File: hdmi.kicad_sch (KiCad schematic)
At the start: 24 parts, among them U14 NTS0102_XSON, U17 PI3HDX511DZLE, U18 74LVC1T45GM

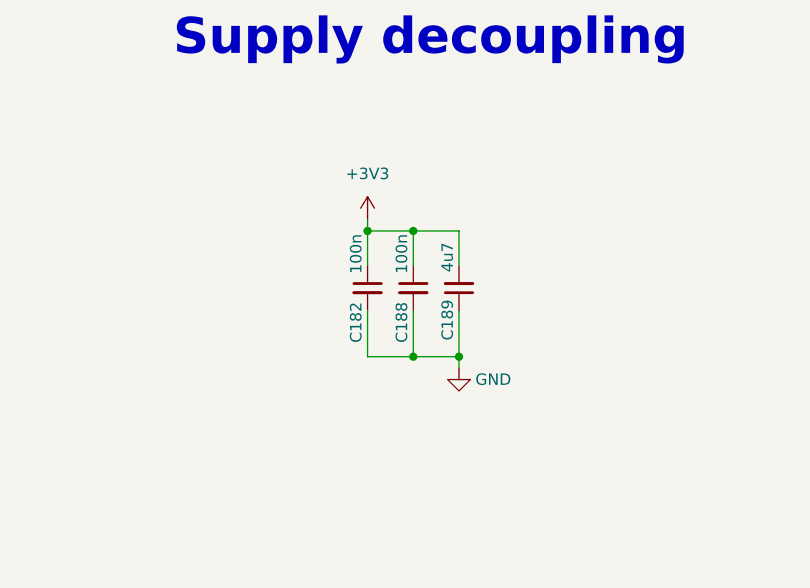
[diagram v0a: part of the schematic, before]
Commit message: [#55860] Add HDMI ferrite bead
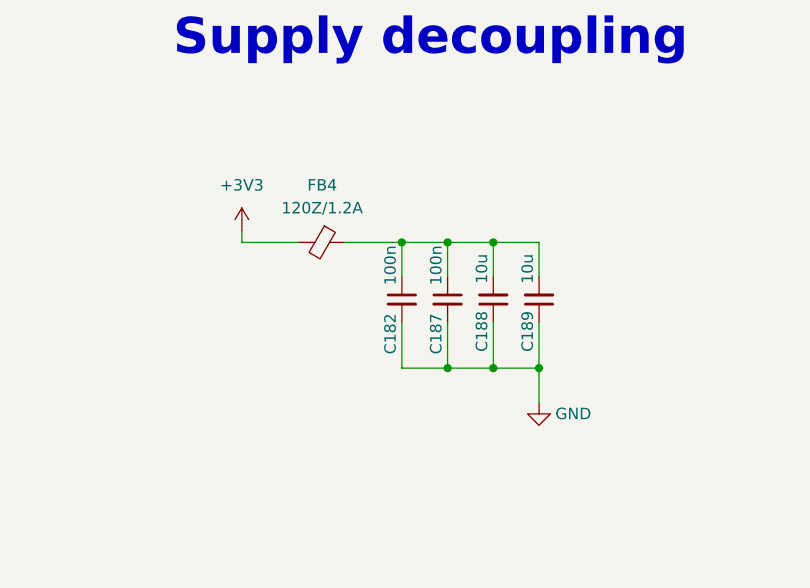
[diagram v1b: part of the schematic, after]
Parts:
- removed C188: C_100n_0201, antmicro-footprints:C_0201, symbol antmicroCapacitorsmisc:C_100n_0201
- removed C189: C_4u7_0402, antmicro-footprints:C_0402_1005Metric, symbol antmicroCapacitors0402:C_4u7_0402
- added C187: C_100n_0201, antmicro-footprints:C_0201, symbol antmicroCapacitorsmisc:C_100n_0201
- added C188, C189: C_10u_10V_0402, antmicro-footprints:C_0402_1005Metric, symbol antmicroCapacitors0402:C_10u_10V_0402
- added FB4: FB_120Z_1.2A_TDK-MPZ_0402, antmicro-footprints:FB_0402_1005Metric, symbol antmicroFerriteBeadsandChips:FB_120Z_1.2A_TDK-MPZ_0402
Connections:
- net +3V3: now also FB4.2; no longer C182.1
- net GND: now also C187.2, C188.1, C189.1
- new net: C182.1, C187.1, C188.2, C189.2, FB4.1

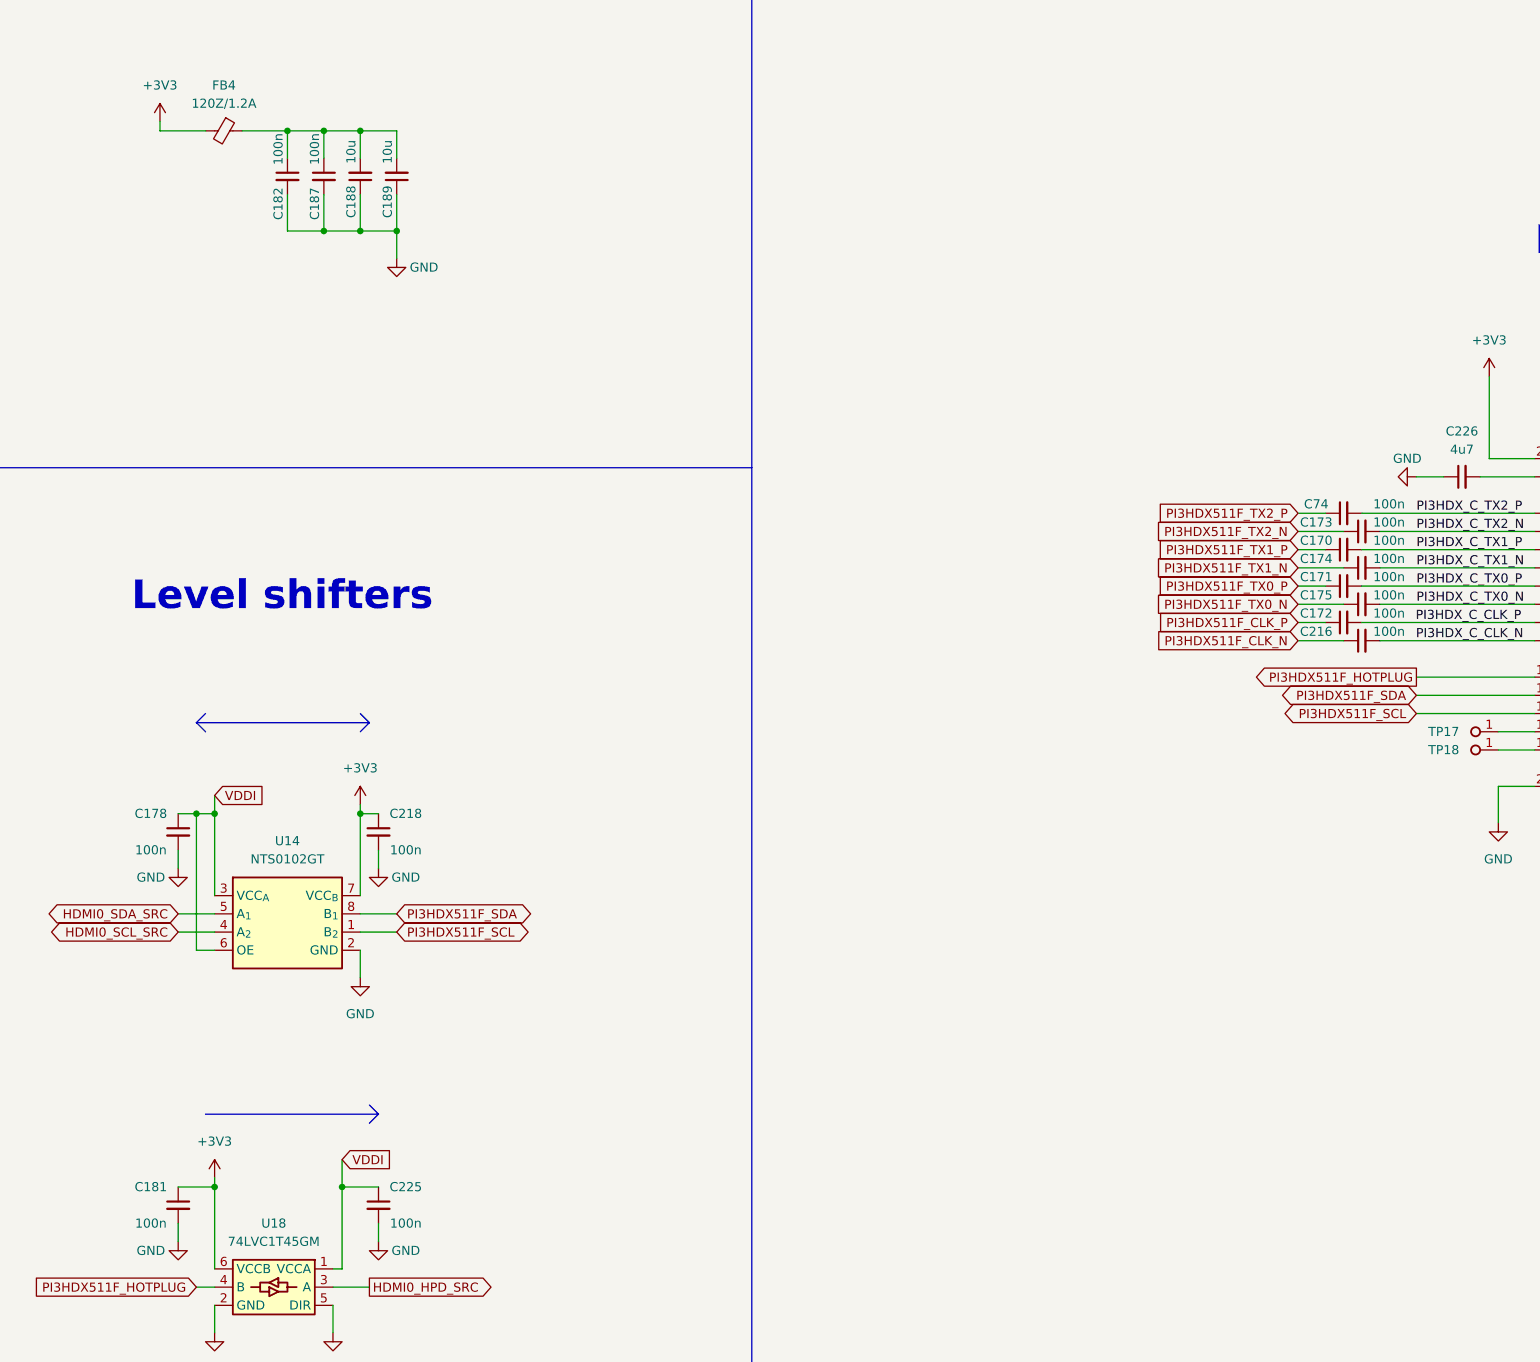
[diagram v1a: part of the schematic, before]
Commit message: [#55992] Replace 100n capacitors
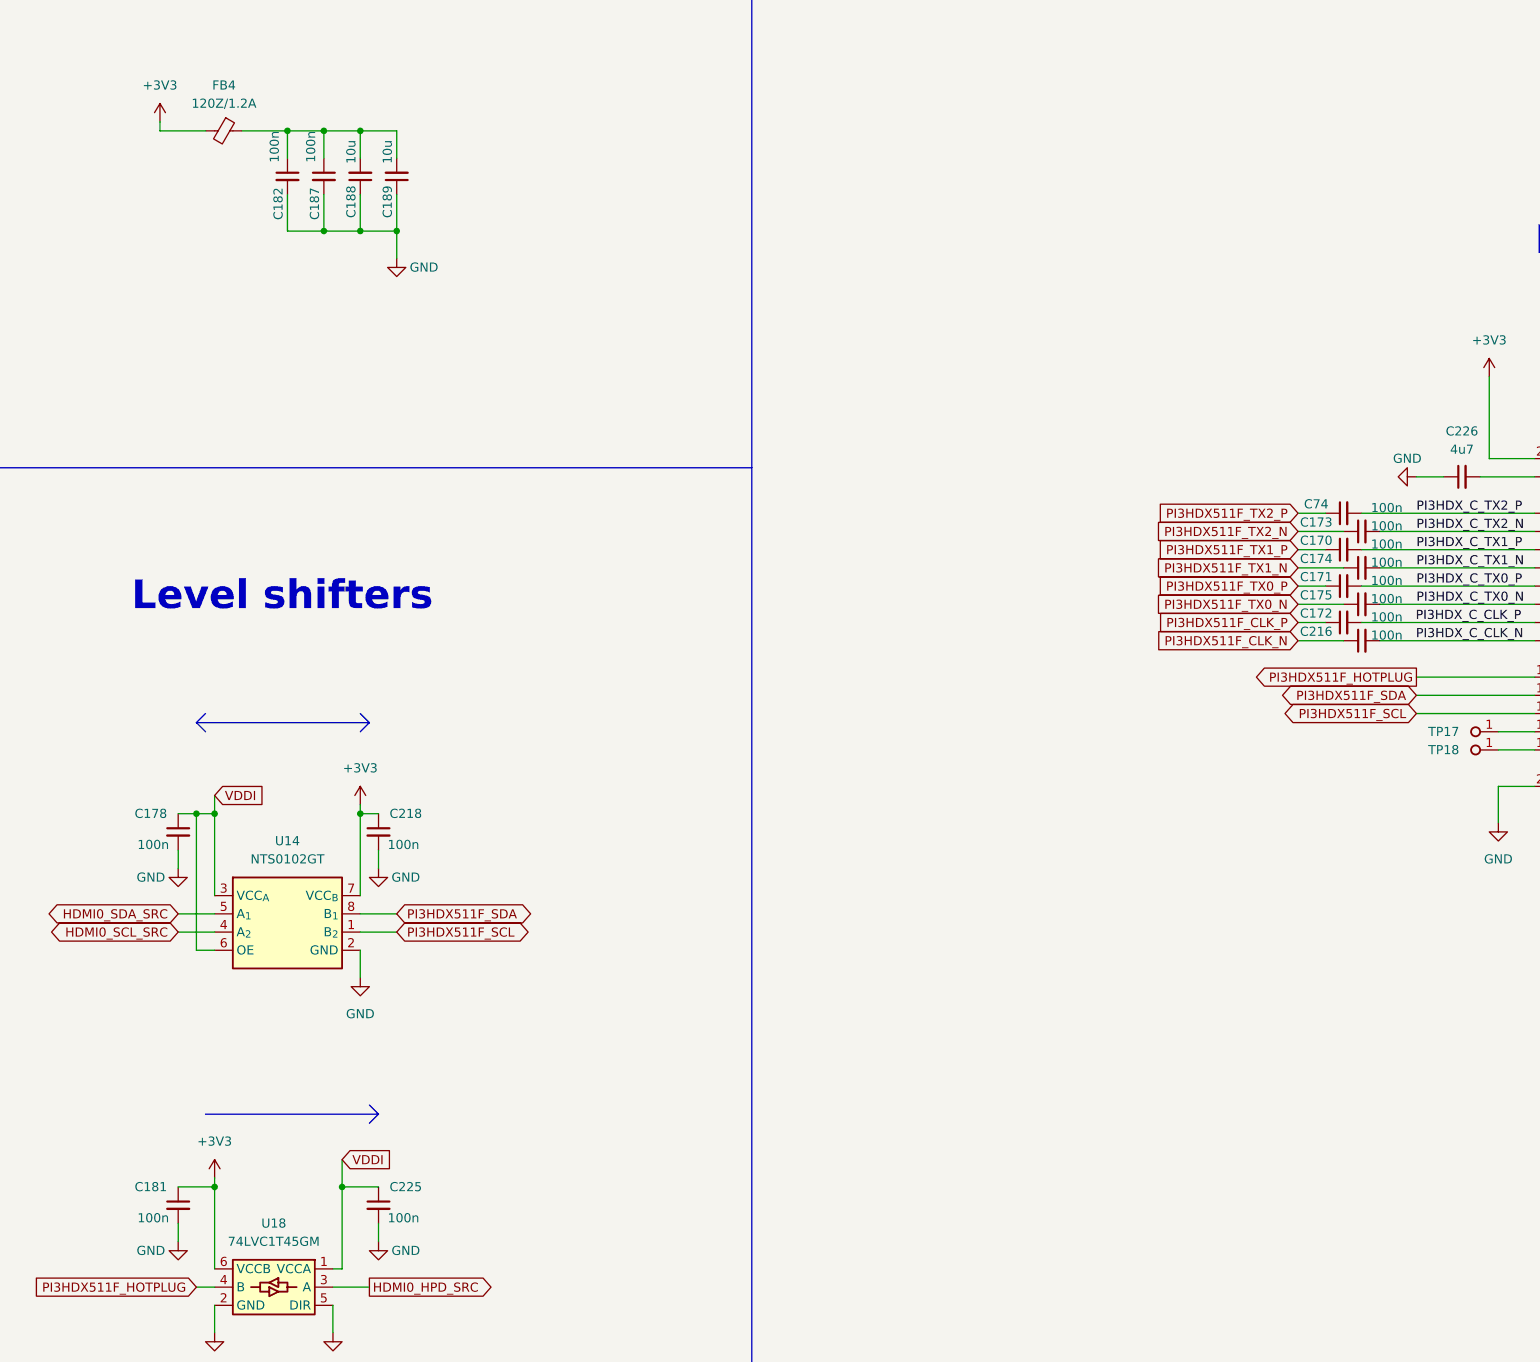
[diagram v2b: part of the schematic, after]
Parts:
- C170, C171, C172, C173, C174, C175, C178, C181, C182, C187, C216, C218, C225, C74: value C_100n_0201 -> C_100n_0402; footprint antmicro-footprints:C_0201 -> antmicro-footprints:C_0402_1005Metric; symbol antmicroCapacitorsmisc:C_100n_0201 -> antmicroCapacitors0402:C_100n_0402; Dielectric (none) -> X5R; MPN CC0201KRX6S5BB104 -> GRM155R61H104KE14D; Manufacturer YAGEO -> Murata; Voltage (none) -> 50V

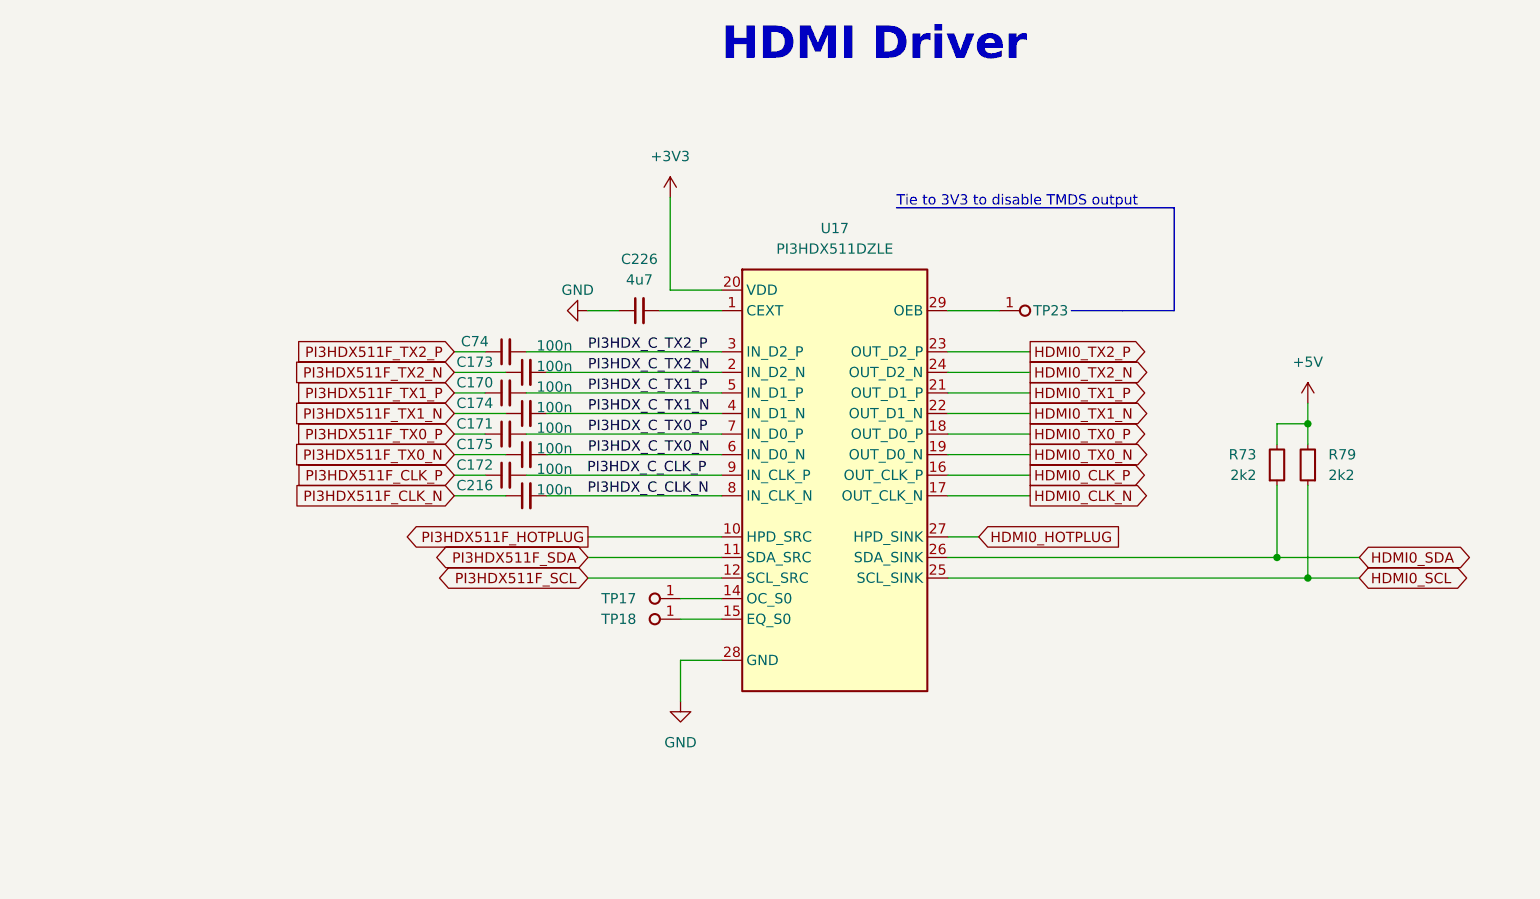
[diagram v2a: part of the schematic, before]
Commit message: [#55860] Update HDMI driver symbol
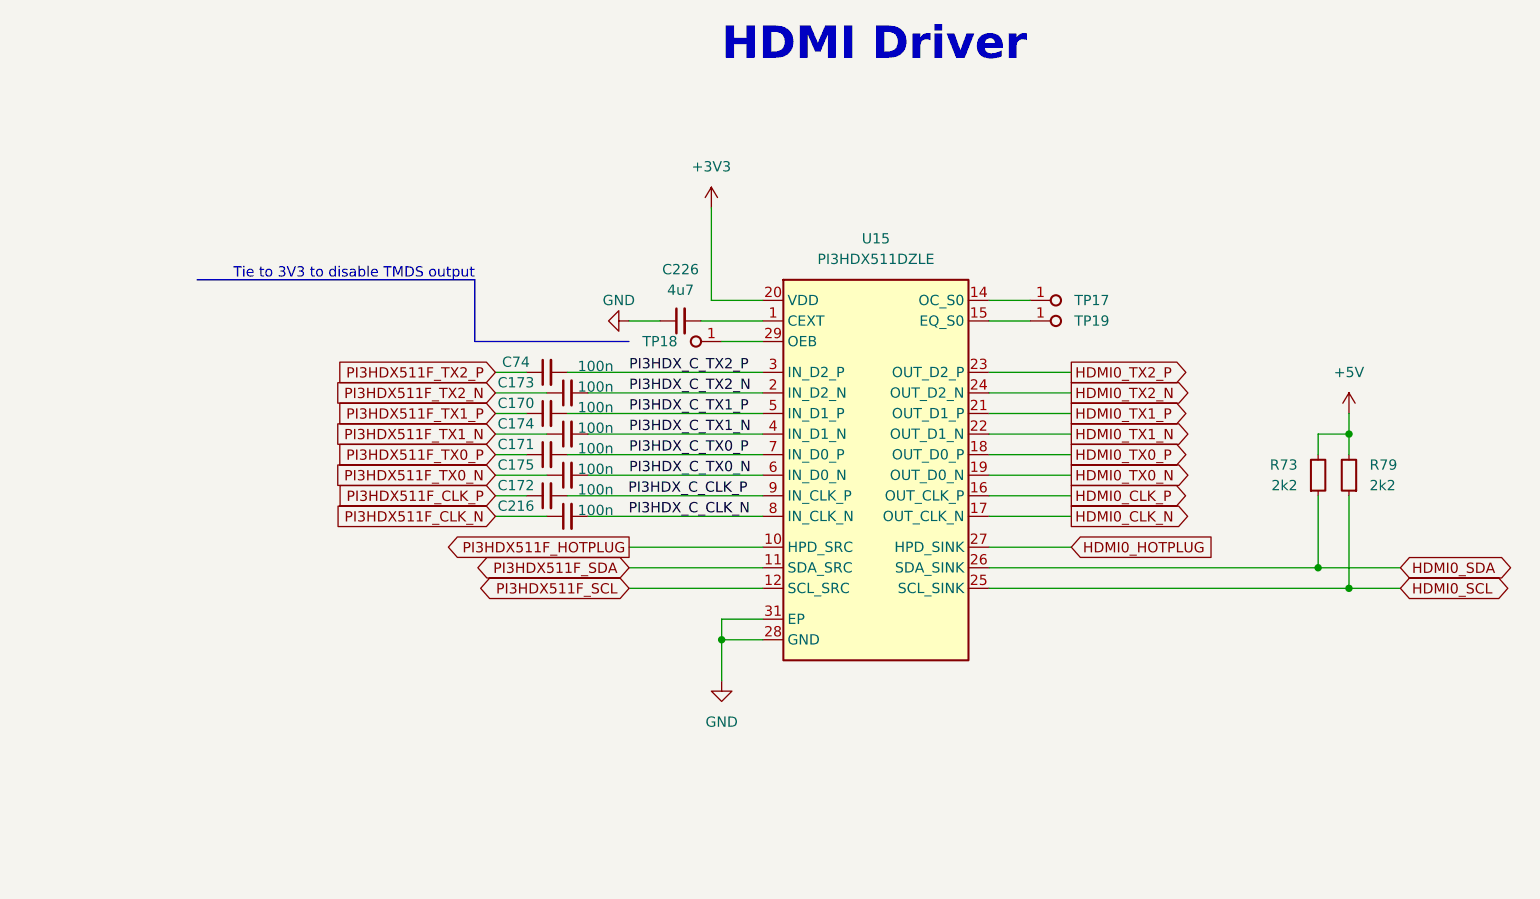
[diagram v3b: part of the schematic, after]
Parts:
- removed TP23: TP_0.75mm_SMD, antmicro-footprints:TP_SMD_0.75mm, symbol antmicroTestPoints:TP_0.75mm_SMD
- removed U17: PI3HDX511DZLE, antmicro-footprints:TQFN-ZL-30, symbol antmicroInterfaceDriversReceiversTransceivers:PI3HDX511DZLE
- added TP19: TP_0.75mm_SMD, antmicro-footprints:TP_SMD_0.75mm, symbol antmicroTestPoints:TP_0.75mm_SMD
- added U15: PI3HDX511DZLE, antmicro-footprints:TQFN-30-1EP_2.5x4.5mm_P0.4mm_Layout5x10, symbol antmicroInterfaceDriversReceiversTransceivers:PI3HDX511DZLE
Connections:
- net +3V3: now also U15.20 (VDD), U15.30 (VDD)
- net GND: now also U15.13 (GND), U15.28 (GND), U15.31 (EP)
- net HDMI0_CLK_N: now also U15.17 (OUT_CLK_N)
- net HDMI0_CLK_P: now also U15.16 (OUT_CLK_P)
- net HDMI0_HOTPLUG: now also U15.27 (HPD_SINK)
- net HDMI0_SCL: now also U15.25 (SCL_SINK)
- net HDMI0_SDA: now also U15.26 (SDA_SINK)
- net HDMI0_TX0_N: now also U15.19 (OUT_D0_N)
- net HDMI0_TX0_P: now also U15.18 (OUT_D0_P)
- net HDMI0_TX1_N: now also U15.22 (OUT_D1_N)
- net HDMI0_TX1_P: now also U15.21 (OUT_D1_P)
- net HDMI0_TX2_N: now also U15.24 (OUT_D2_N)
- net HDMI0_TX2_P: now also U15.23 (OUT_D2_P)
- net PI3HDX511F_HOTPLUG: now also U15.10 (HPD_SRC)
- net PI3HDX511F_SCL: now also U15.12 (SCL_SRC)
- net PI3HDX511F_SDA: now also U15.11 (SDA_SRC)
- net PI3HDX_C_CLK_N: now also U15.8 (IN_CLK_N)
- net PI3HDX_C_CLK_P: now also U15.9 (IN_CLK_P)
- net PI3HDX_C_TX0_N: now also U15.6 (IN_D0_N)
- net PI3HDX_C_TX0_P: now also U15.7 (IN_D0_P)
- net PI3HDX_C_TX1_N: now also U15.4 (IN_D1_N)
- net PI3HDX_C_TX1_P: now also U15.5 (IN_D1_P)
- net PI3HDX_C_TX2_N: now also U15.2 (IN_D2_N)
- net PI3HDX_C_TX2_P: now also U15.3 (IN_D2_P)
- net at TP17.1: now also U15.14 (OC_S0)
- net at C226.2: now also U15.1 (CEXT)
- net at TP18.1: now also U15.29 (OEB)
- new net: TP19.1, U15.15 (EQ_S0)
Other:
- moved on the sheet: C170, C171, C172, C173, C174, C175, C216, C226, C74, R73, R79, TP17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
